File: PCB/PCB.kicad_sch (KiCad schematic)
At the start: 1 part, among them U1 ESP32-DEVKIT-V1

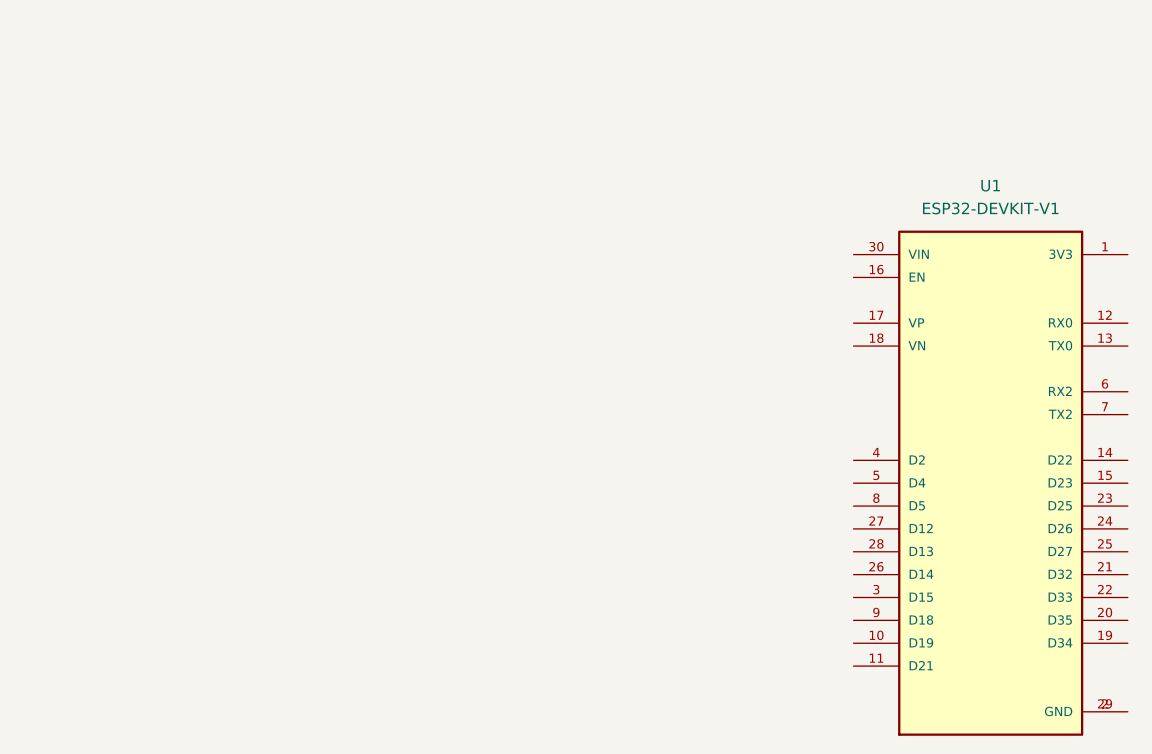
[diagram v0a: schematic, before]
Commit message: Correccion agujeros PCB
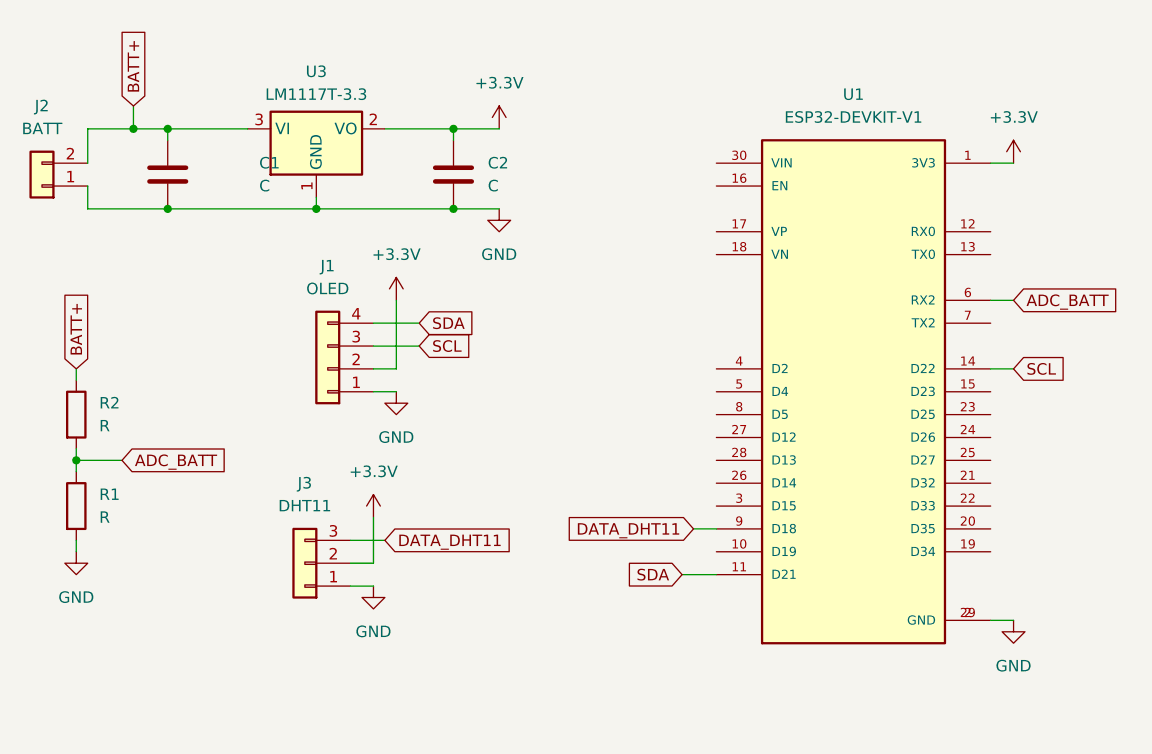
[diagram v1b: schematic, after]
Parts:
- added C1, C2: C, Capacitor_THT:CP_Radial_D5.0mm_P2.50mm, symbol Device:C
- added J1: OLED, Connector_PinHeader_2.54mm:PinHeader_1x04_P2.54mm_Vertical, symbol Connector_Generic:Conn_01x04
- added J2: BATT, Connector_JST:JST_XH_B2B-XH-A_1x02_P2.50mm_Vertical, symbol Connector_Generic:Conn_01x02
- added J3: DHT11, Connector_PinHeader_2.54mm:PinHeader_1x03_P2.54mm_Vertical, symbol Connector_Generic:Conn_01x03
- added R1, R2: R, Resistor_THT:R_Axial_DIN0309_L9.0mm_D3.2mm_P15.24mm_Horizontal, symbol Device:R
- added U3: LM1117T-3.3, Package_TO_SOT_THT:TO-220-3_Horizontal_TabDown, symbol Regulator_Linear:LM1117T-3.3
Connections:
- net +3.3V: now reaches U1.1 (3V3)
- net +3.3V: now also C2.1, J1.2 (Pin_2), J3.2 (Pin_2), U3.2 (VO)
- net SDA: now reaches U1.11 (D21)
- net SDA: now also J1.4 (Pin_4)
- net SCL: now reaches U1.14 (D22)
- net SCL: now also J1.3 (Pin_3)
- net GND: now reaches U1.2 (GND), U1.29 (GND)
- net GND: now also C1.2, C2.2, J1.1 (Pin_1), J2.1 (Pin_1), J3.1 (Pin_1), R1.2, U3.1 (GND)
- net ADC_BATT: now reaches U1.6 (RX2)
- net ADC_BATT: now also R1.1, R2.2
- net DATA_DHT11: now reaches U1.9 (D18)
- net DATA_DHT11: now also J3.3 (Pin_3)
- new net BATT+: C1.1, J2.2 (Pin_2), R2.1, U3.3 (VI)
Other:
- moved on the sheet: U1
